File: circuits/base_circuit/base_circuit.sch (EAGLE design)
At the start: 33 parts, among them U1 ARDUINO-MEGAFULL

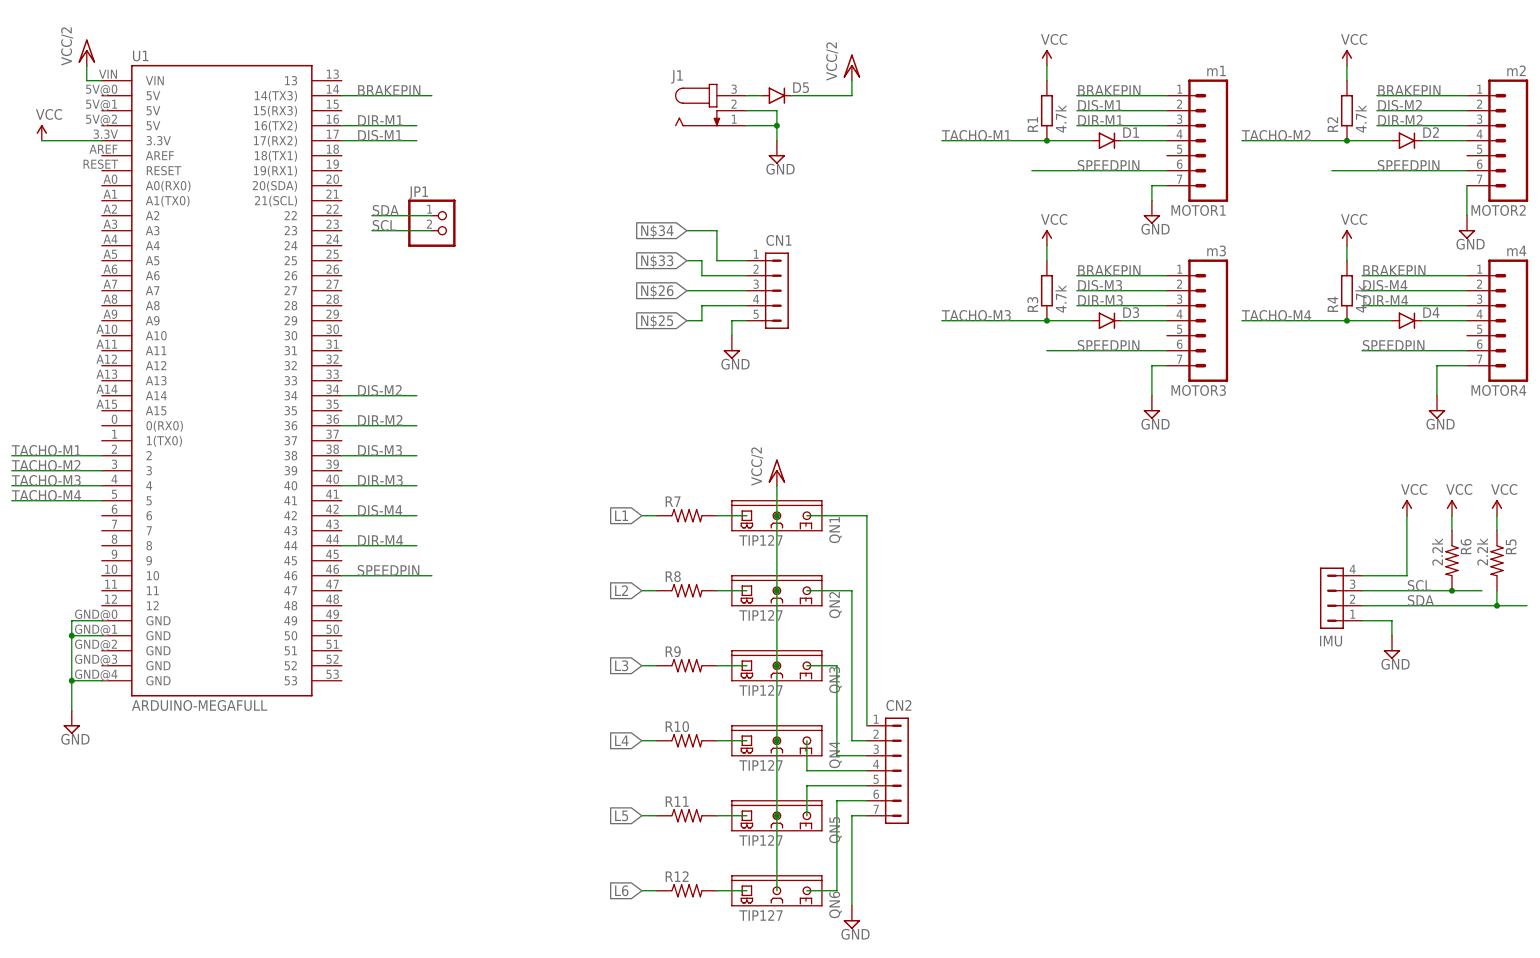
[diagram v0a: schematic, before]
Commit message: changed the whole circuit to use speed control for individula motors and also added connections for top plate design leds
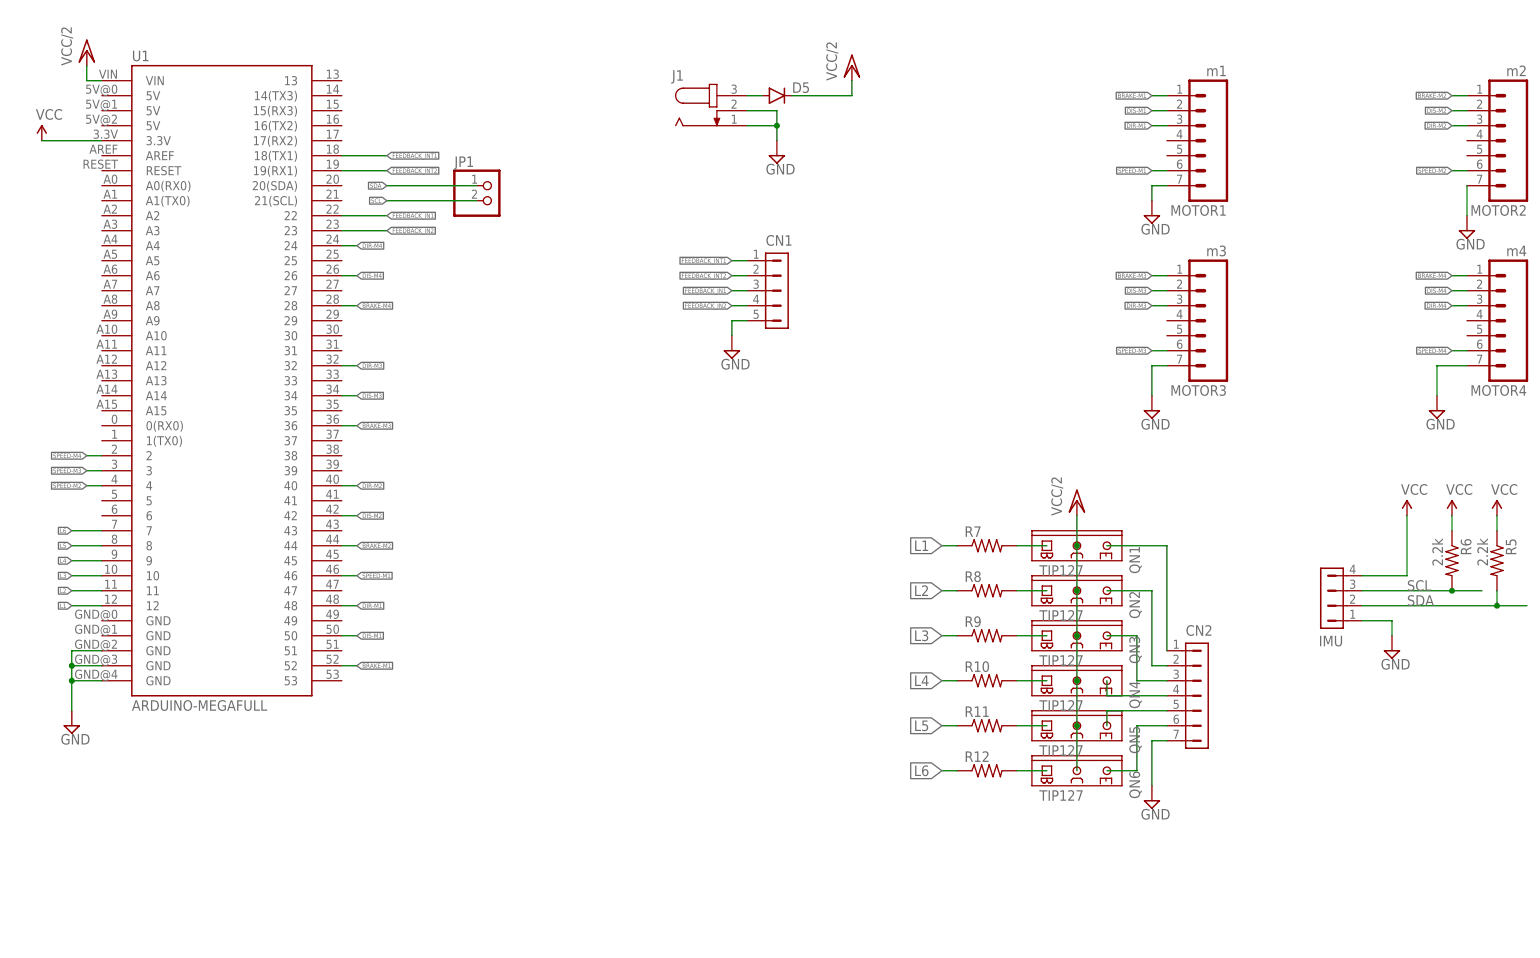
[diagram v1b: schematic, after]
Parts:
- removed D1, D2, D3, D4: (no value), diode4:DIODE1N4148
- removed R1, R2, R3, R4: 4.7k, rcl:R-EU_0207/12
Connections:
- removed net BRAKEPIN: MOTOR1.1, MOTOR2.1, MOTOR3.1, MOTOR4.1, U1.14(TX3)
- removed net N$1: D1.C, MOTOR1.4
- removed net N$2: D2.C, MOTOR2.4
- removed net N$25: CN1.4
- removed net N$26: CN1.3
- removed net N$3: D3.C, MOTOR3.4
- removed net N$33: CN1.2
- removed net N$34: CN1.1
- removed net N$4: D4.C, MOTOR4.4
- removed net SPEEDPIN: MOTOR1.6, MOTOR2.6, MOTOR3.6, MOTOR4.6, U1.46
- removed net TACHO-M1: D1.A, R1.1, U1.2
- removed net TACHO-M2: D2.A, R2.1, U1.3
- removed net TACHO-M3: D3.A, R3.1, U1.4
- removed net TACHO-M4: D4.A, R4.1, U1.5
- new net BRAKE-M1: MOTOR1.1, U1.52
- new net BRAKE-M2: MOTOR2.1, U1.44
- new net BRAKE-M3: MOTOR3.1, U1.36
- new net BRAKE-M4: MOTOR4.1, U1.28
- new net FEEDBACK_IN1: CN1.3, U1.22
- new net FEEDBACK_IN2: CN1.4, U1.23
- new net FEEDBACK_INT1: CN1.1, U1.18(TX1)
- new net FEEDBACK_INT2: CN1.2, U1.19(RX1)
- new net SPEED-M1: MOTOR1.6, U1.46
- new net SPEED-M2: MOTOR2.6, U1.4
- new net SPEED-M3: MOTOR3.6, U1.3
- new net SPEED-M4: MOTOR4.6, U1.2
- net DIR-M1: now also U1.48; no longer U1.16(TX2)
- net DIR-M2: now also U1.40; no longer U1.36
- net DIR-M3: now also U1.32; no longer U1.40
- net DIR-M4: now also U1.24; no longer U1.44
- net DIS-M1: now also U1.50; no longer U1.17(RX2)
- net DIS-M2: now also U1.42; no longer U1.34
- net DIS-M3: now also U1.34; no longer U1.38
- net DIS-M4: now also U1.26; no longer U1.42
- net GND: now also U1.GND@2, U1.GND@3; no longer U1.GND@0, U1.GND@1
- net L1: now also U1.12
- net L2: now also U1.11
- net L3: now also U1.10
- net L4: now also U1.9
- net L5: now also U1.8
- net L6: now also U1.7
- net VCC: no longer R1.2, R2.2, R3.2, R4.2
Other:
- note removed: "RPlidar Servo"
- moved on the sheet: CN2, JP1, QN1, QN2, QN3, QN4, QN5, QN6, R10, R11, R12, R7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
